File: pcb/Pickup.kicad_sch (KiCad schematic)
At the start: 42 parts, among them IC1 MAX9924UAUB+, Q7 MMBT2222A, T1 SM-LP-5001E, U4 AT223-CuH-S

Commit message: changed zener footprints
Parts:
- Z2: footprint SamacSys_Parts:BZT52B5V1E308 -> Diode_SMD:D_SOD-123
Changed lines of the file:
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@@
 			)
 		)
-		(property "Footprint" "SamacSys_Parts:BZT52B5V1E308"
+		(property "Footprint" "Diode_SMD:D_SOD-123"
 			(at 209.55 92.71 0)
 			(effects

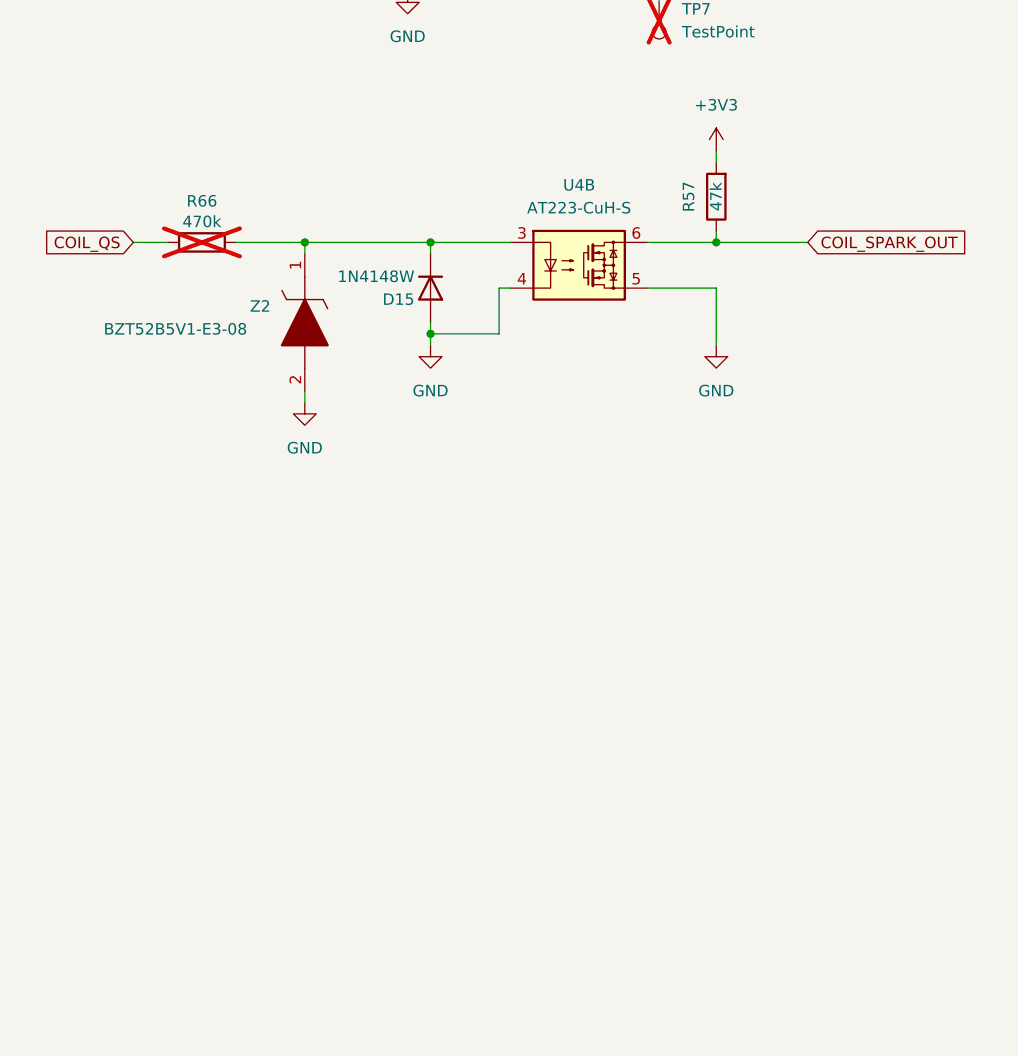
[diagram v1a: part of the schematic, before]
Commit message: added PVL ignitions support
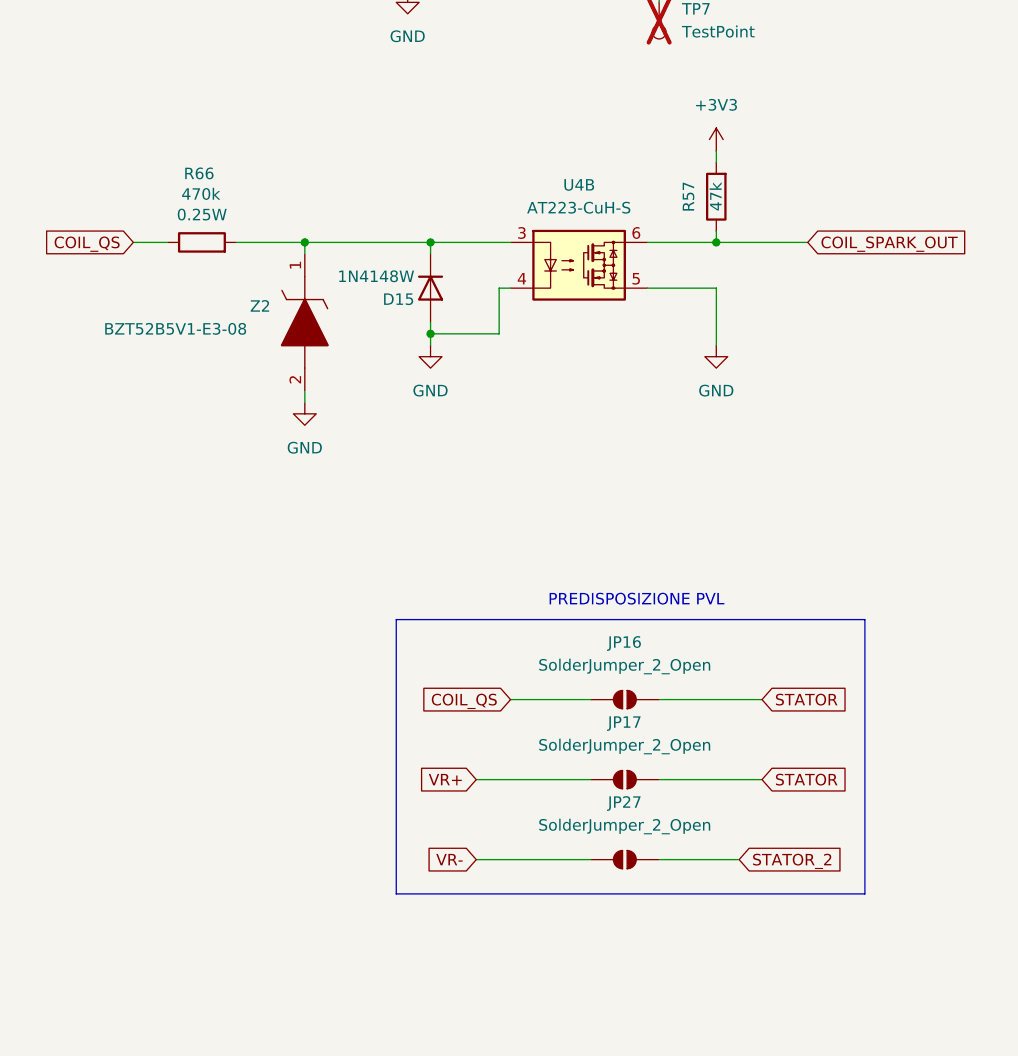
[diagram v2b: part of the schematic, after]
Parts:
- added JP16, JP17, JP27: SolderJumper_2_Open, Jumper:SolderJumper-2_P1.3mm_Open_RoundedPad1.0x1.5mm, symbol Jumper:SolderJumper_2_Open
- R66: footprint Resistor_THT:R_Axial_DIN0204_L3.6mm_D1.6mm_P1.90mm_Vertical -> Resistor_SMD:R_0805_2012Metric; now fitted
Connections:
- net COIL_QS: now also R66.1, JP16.2 (B); no longer R66.2
- net VR+: now also JP17.2 (B)
- net VR-: now also JP27.2 (B)
- net at D15.1 (K), U4.3, Z2.1: now also R66.2; no longer R66.1
- new net STATOR: JP16.1 (A), JP17.1 (A)
- new net STATOR_2: JP27.1 (A)
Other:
- note added: "PREDISPOSIZIONE PVL"

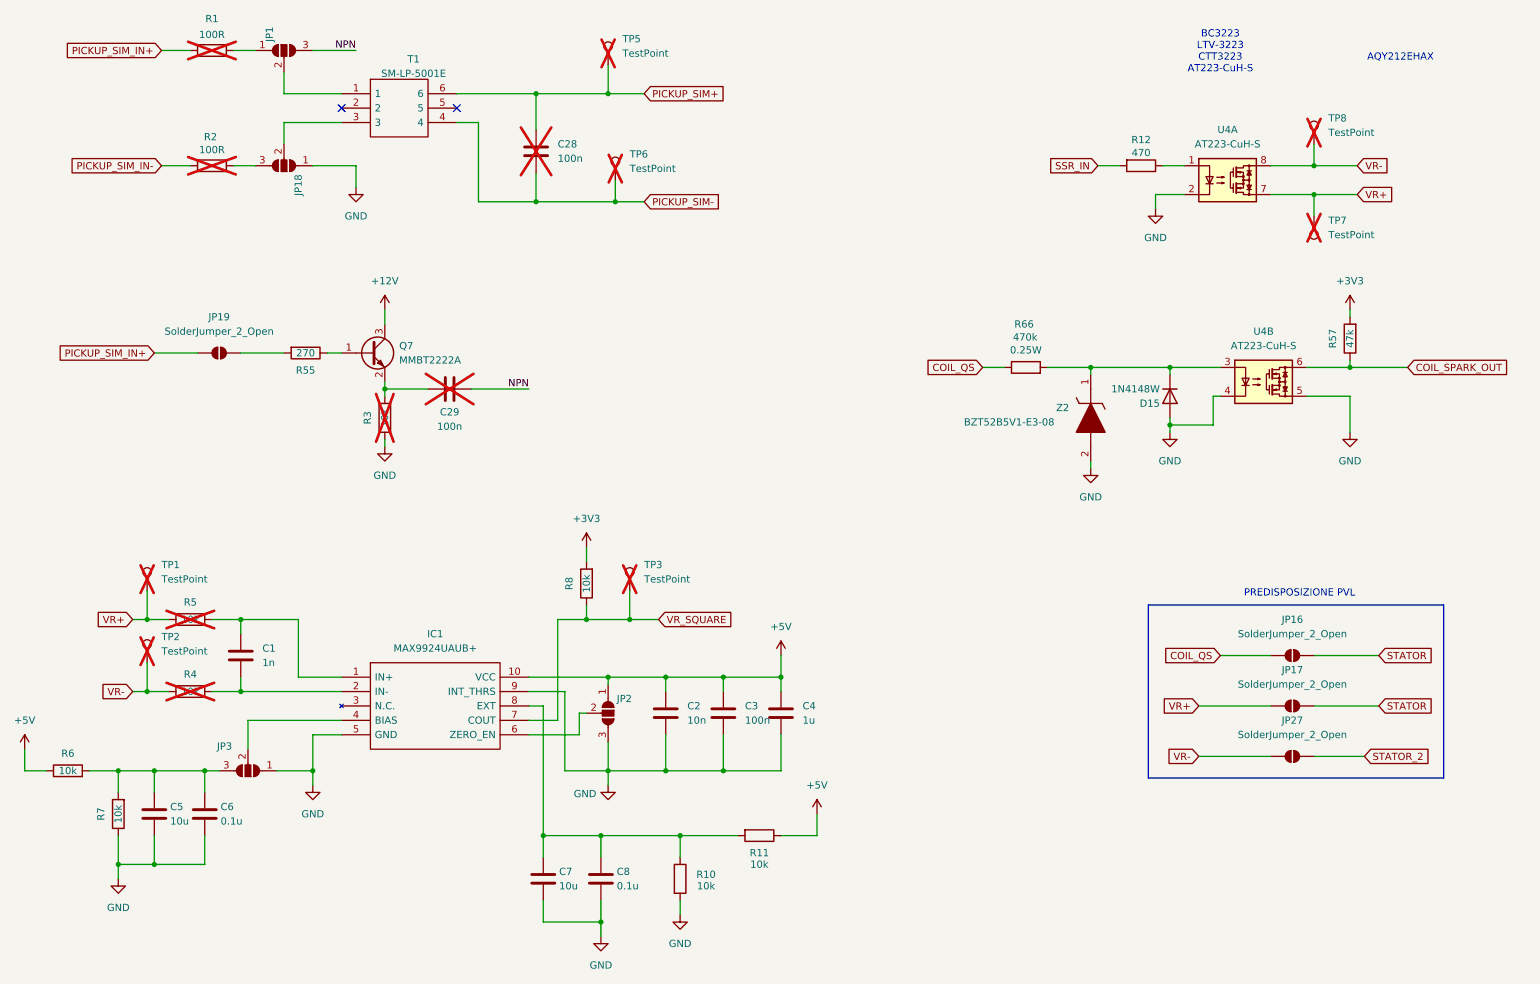
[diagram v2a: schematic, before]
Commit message: changed THT to SMD for both resistors and capacitors since they will be replaced by hand with soldering tweezers
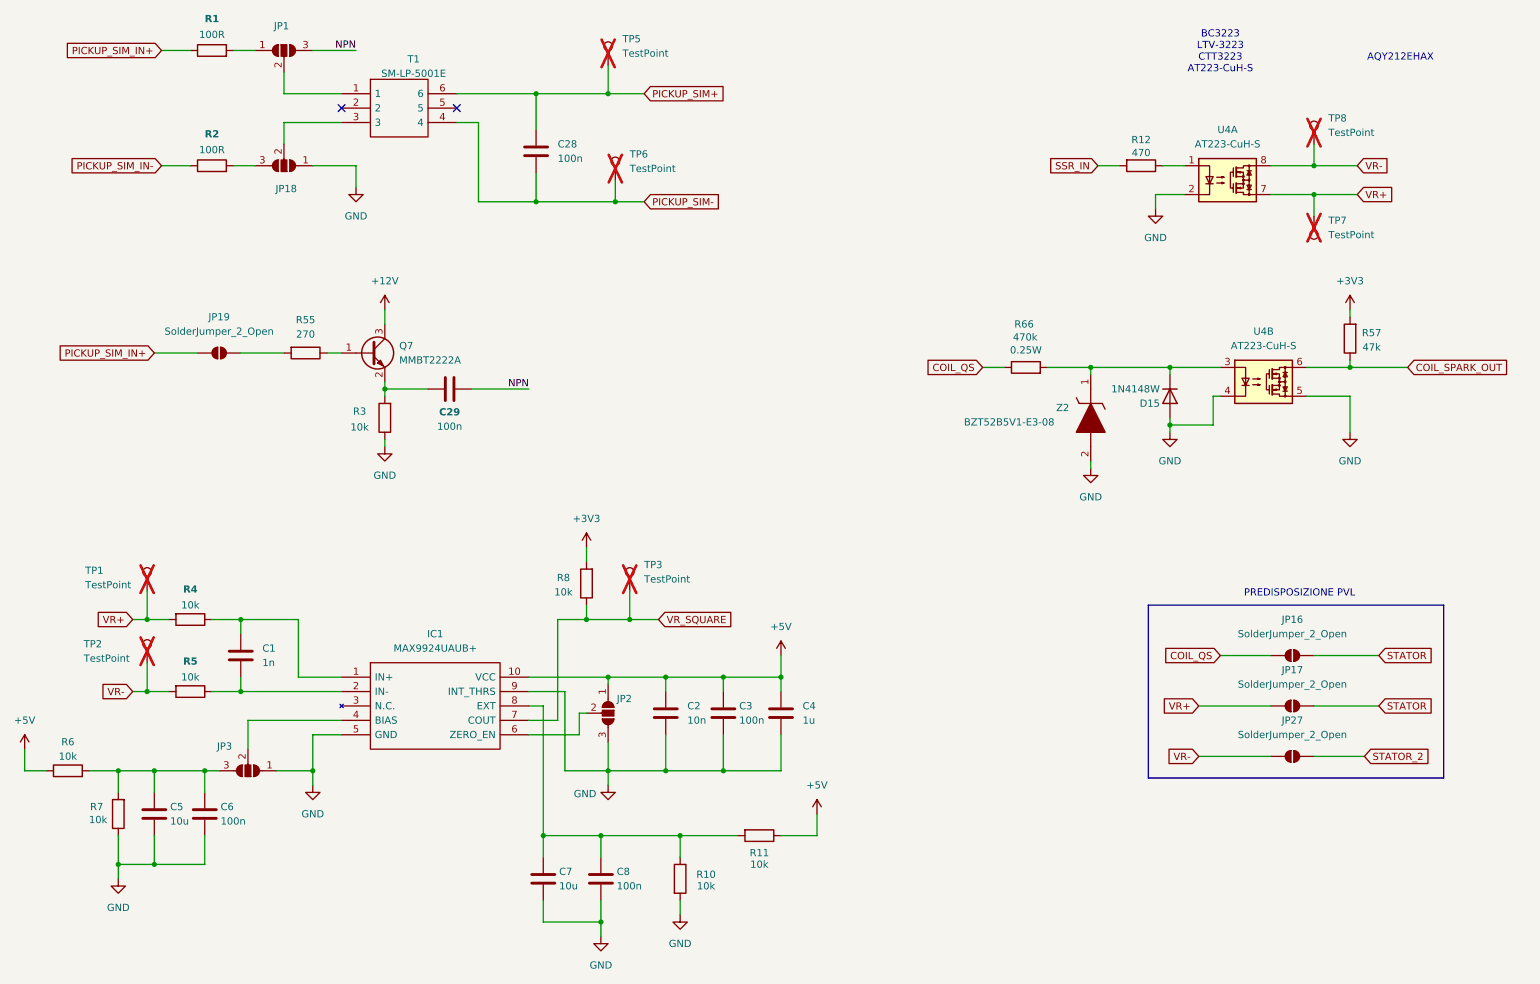
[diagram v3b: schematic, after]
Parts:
- C28, C29: footprint Capacitor_THT:C_Disc_D4.3mm_W1.9mm_P5.00mm -> Capacitor_SMD:C_0603_1608Metric; now fitted
- C6, C8: value 0.1u -> 100n
- R1, R2, R3, R4, R5: footprint Resistor_THT:R_Axial_DIN0204_L3.6mm_D1.6mm_P1.90mm_Vertical -> Resistor_SMD:R_0603_1608Metric; now fitted
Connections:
- net NPN: now also C29.1; no longer C29.2
- net VR+: now also R4.2; no longer R5.1
- net VR-: now also R5.2; no longer R4.1
- net at C1.1, IC1.1 (IN+): now also R4.1; no longer R5.2
- net at C1.2, IC1.2 (IN-): now also R5.1; no longer R4.2
- net at Q7.2 (E), R3.2: now also C29.2; no longer C29.1

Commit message: revision 2.0: changed components numeration
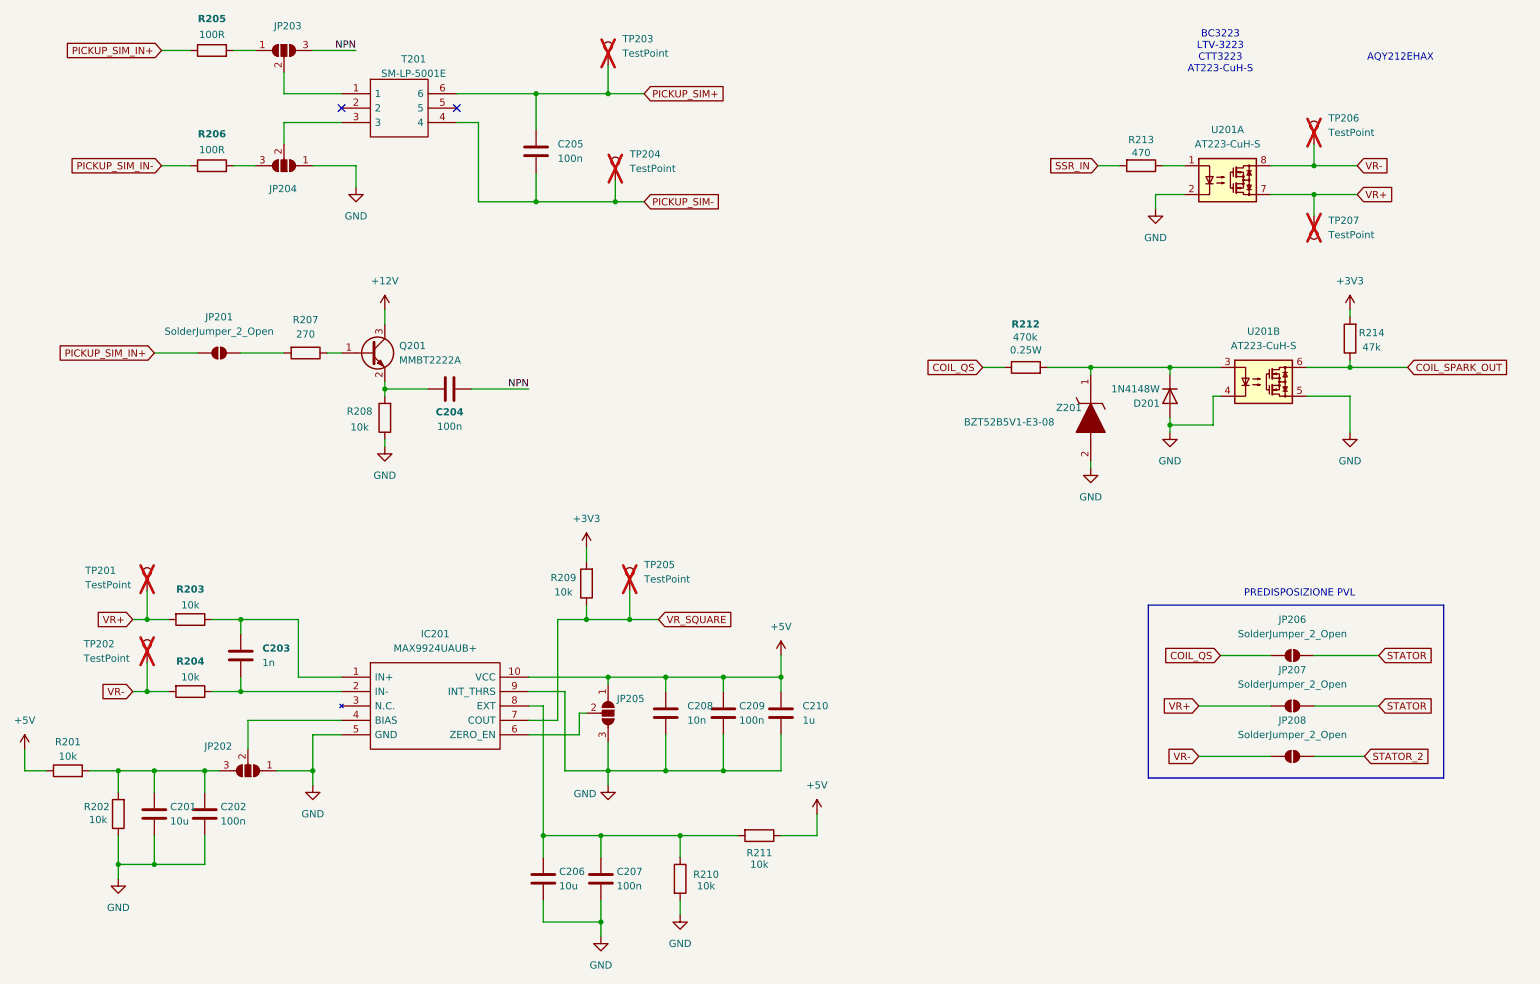
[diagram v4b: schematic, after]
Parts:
- C203: renamed from C1; footprint Capacitor_SMD:C_0603_1608Metric -> Capacitor_SMD:C_0805_2012Metric
- C204: renamed from C29; footprint Capacitor_SMD:C_0603_1608Metric -> Capacitor_SMD:C_0805_2012Metric
- R203: renamed from R4; footprint Resistor_SMD:R_0603_1608Metric -> Resistor_SMD:R_0805_2012Metric
- R204: renamed from R5; footprint Resistor_SMD:R_0603_1608Metric -> Resistor_SMD:R_0805_2012Metric
- R205: renamed from R1; footprint Resistor_SMD:R_0603_1608Metric -> Resistor_SMD:R_0805_2012Metric
- R206: renamed from R2; footprint Resistor_SMD:R_0603_1608Metric -> Resistor_SMD:R_0805_2012Metric
- renumbered C5 to C201, C6 to C202, C28 to C205, C7 to C206, C8 to C207, C2 to C208, C3 to C209, C4 to C210, D15 to D201, IC1 to IC201, JP19 to JP201, JP3 to JP202, JP1 to JP203, JP18 to JP204, JP2 to JP205, JP16 to JP206, JP17 to JP207, JP27 to JP208, Q7 to Q201, R6 to R201, R7 to R202, R55 to R207, R3 to R208, R8 to R209, R10 to R210, R11 to R211, R66 to R212, R12 to R213, R57 to R214, T1 to T201, TP1 to TP201, TP2 to TP202, TP5 to TP203, TP6 to TP204, TP3 to TP205, TP8 to TP206, TP7 to TP207, U4 to U201, Z2 to Z201

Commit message: revision 2.0: changed R and C footprints to 0805 (imperial)
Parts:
- C201, C202, C205, C206, C207, C208, C209, C210: footprint Capacitor_SMD:C_0603_1608Metric -> Capacitor_SMD:C_0805_2012Metric
- R201, R202, R207, R208, R209, R210, R211, R213, R214: footprint Resistor_SMD:R_0603_1608Metric -> Resistor_SMD:R_0805_2012Metric
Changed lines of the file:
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@@
 			)
 		)
-		(property "Footprint" "Resistor_SMD:R_0603_1608Metric"
+		(property "Footprint" "Resistor_SMD:R_0805_2012Metric"
 			(at 25.4 154.178 90)
 			(effects
@@
 			)
 		)
-		(property "Footprint" "Capacitor_SMD:C_0603_1608Metric"
+		(property "Footprint" "Capacitor_SMD:C_0805_2012Metric"
 			(at 110.1852 175.26 0)
 			(effects
@@
 			)
 		)
-		(property "Footprint" "Capacitor_SMD:C_0603_1608Metric"
+		(property "Footprint" "Capacitor_SMD:C_0805_2012Metric"
 			(at 120.3452 175.26 0)
 			(effects
@@
 			)
 		)
-		(property "Footprint" "Resistor_SMD:R_0603_1608Metric"
+		(property "Footprint" "Resistor_SMD:R_0805_2012Metric"
 			(at 214.63 43.942 90)
 			(effects
@@
 			)
 		)
-		(property "Footprint" "Resistor_SMD:R_0603_1608Metric"
+		(property "Footprint" "Resistor_SMD:R_0805_2012Metric"
 			(at 36.068 160.02 90)
 			(effects
@@
 			)
 		)
-		(property "Footprint" "Capacitor_SMD:C_0603_1608Metric"
+		(property "Footprint" "Capacitor_SMD:C_0805_2012Metric"
 			(at 152.0952 146.05 0)
 			(effects
@@
 			)
 		)
-		(property "Footprint" "Capacitor_SMD:C_0603_1608Metric"
+		(property "Footprint" "Capacitor_SMD:C_0805_2012Metric"
 			(at 108.9152 46.99 0)
 			(effects
@@
 			)
 		)
-		(property "Footprint" "Resistor_SMD:R_0603_1608Metric"
+		(property "Footprint" "Resistor_SMD:R_0805_2012Metric"
 			(at 67.31 76.962 90)
 			(effects
@@
 			)
 		)
-		(property "Footprint" "Resistor_SMD:R_0603_1608Metric"
+		(property "Footprint" "Resistor_SMD:R_0805_2012Metric"
 			(at 118.618 119.38 90)
 			(effects
@@
 			)
 		)
-		(property "Footprint" "Resistor_SMD:R_0603_1608Metric"
+		(property "Footprint" "Resistor_SMD:R_0805_2012Metric"
 			(at 253.238 76.2 90)
 			(effects
@@
 			)
 		)
-		(property "Footprint" "Capacitor_SMD:C_0603_1608Metric"
+		(property "Footprint" "Capacitor_SMD:C_0805_2012Metric"
 			(at 131.7752 146.05 0)
 			(effects
@@
 			)
 		)
-		(property "Footprint" "Capacitor_SMD:C_0603_1608Metric"
+		(property "Footprint" "Capacitor_SMD:C_0805_2012Metric"
 			(at 141.9352 146.05 0)
 			(effects
@@
 			)
 		)
-		(property "Footprint" "Resistor_SMD:R_0603_1608Metric"
+		(property "Footprint" "Resistor_SMD:R_0805_2012Metric"
 			(at 83.058 90.17 90)
 			(effects
@@
 			)
 		)
-		(property "Footprint" "Capacitor_SMD:C_0603_1608Metric"
+		(property "Footprint" "Capacitor_SMD:C_0805_2012Metric"
 			(at 41.6052 163.83 0)
 			(effects
@@
 			)
 		)
-		(property "Footprint" "Resistor_SMD:R_0603_1608Metric"
+		(property "Footprint" "Resistor_SMD:R_0805_2012Metric"
 			(at 147.32 162.052 90)
 			(effects
@@
 			)
 		)
-		(property "Footprint" "Capacitor_SMD:C_0603_1608Metric"
+		(property "Footprint" "Capacitor_SMD:C_0805_2012Metric"
 			(at 50.4952 163.83 0)
 			(effects
@@
 			)
 		)
-		(property "Footprint" "Resistor_SMD:R_0603_1608Metric"
+		(property "Footprint" "Resistor_SMD:R_0805_2012Metric"
 			(at 131.572 171.45 90)
 			(effects
